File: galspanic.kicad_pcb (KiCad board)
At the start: 2 copper layers, 86.5 x 150 mm, 26 parts, among them J1 x68000_expansion, U1 CY62167E, U10 SN74AHCT245, U11 SN74AHCT245, U2 CY62167E, U3 CY62167E, U4 CY62167E, U5 ATF22V10C-10PU, U6 SN74AHCT245, U7 SN74AHCT245, U8 SN74AHCT245, U9 SN74AHCT245

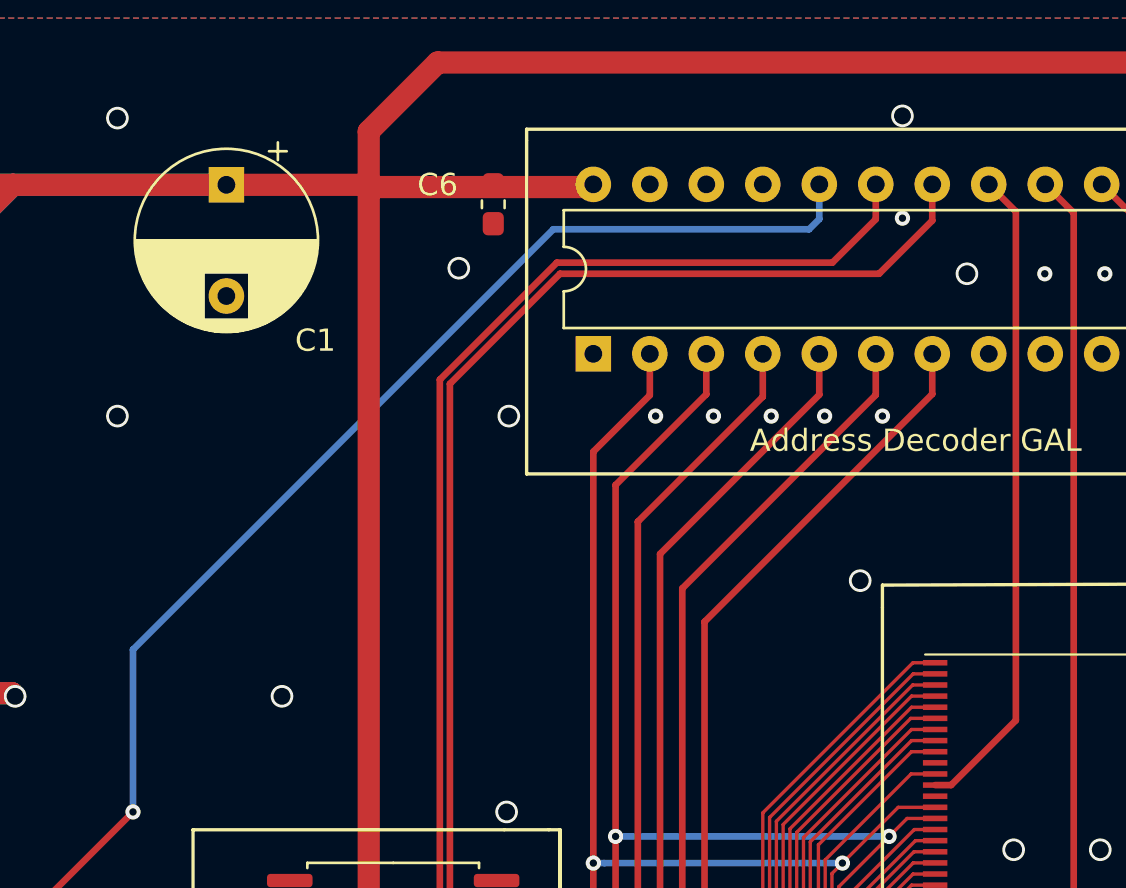
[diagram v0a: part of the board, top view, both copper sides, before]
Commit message: route A20, fix power cap footprint
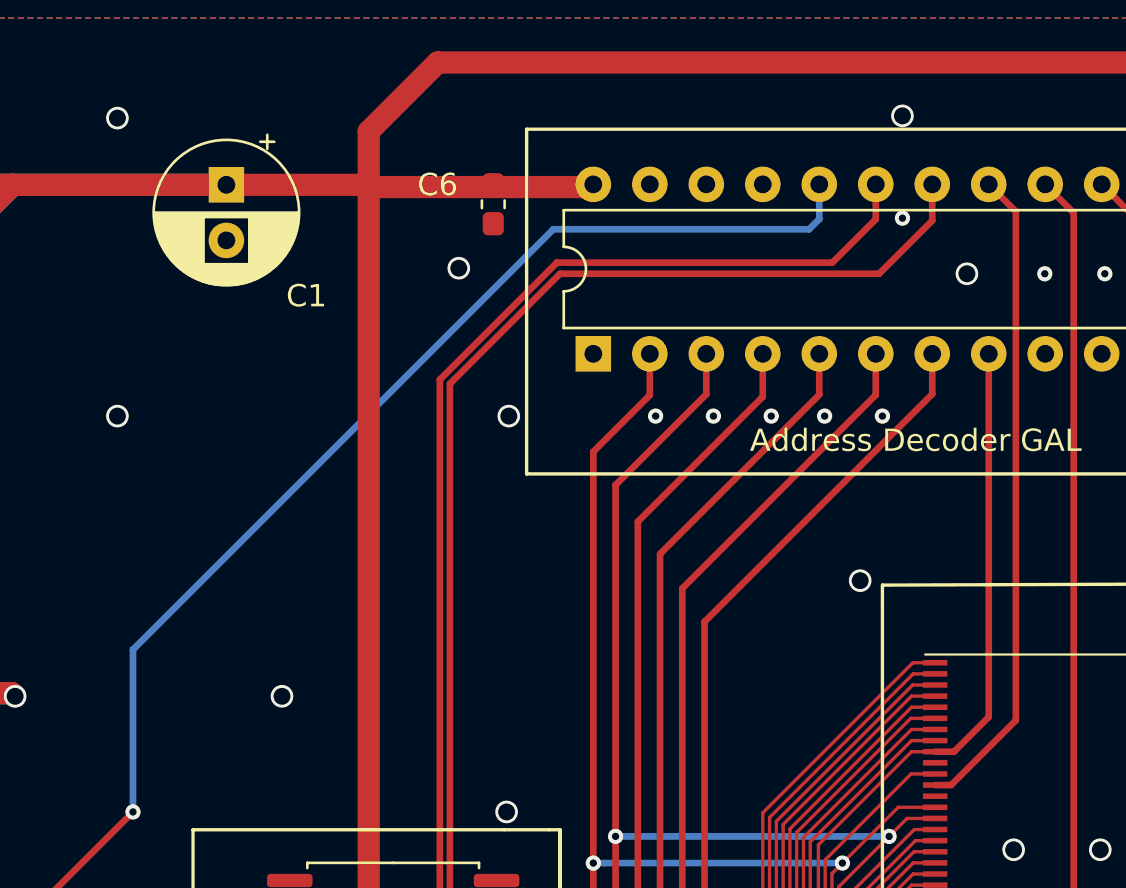
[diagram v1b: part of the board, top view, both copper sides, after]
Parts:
- C1: footprint Capacitor_THT:CP_Radial_D8.0mm_P5.00mm -> Capacitor_THT:CP_Radial_D6.3mm_P2.50mm
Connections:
- U5 pad 8: GND -> /A20
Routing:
- net /A20: track 116.5 -> 135.9 mm

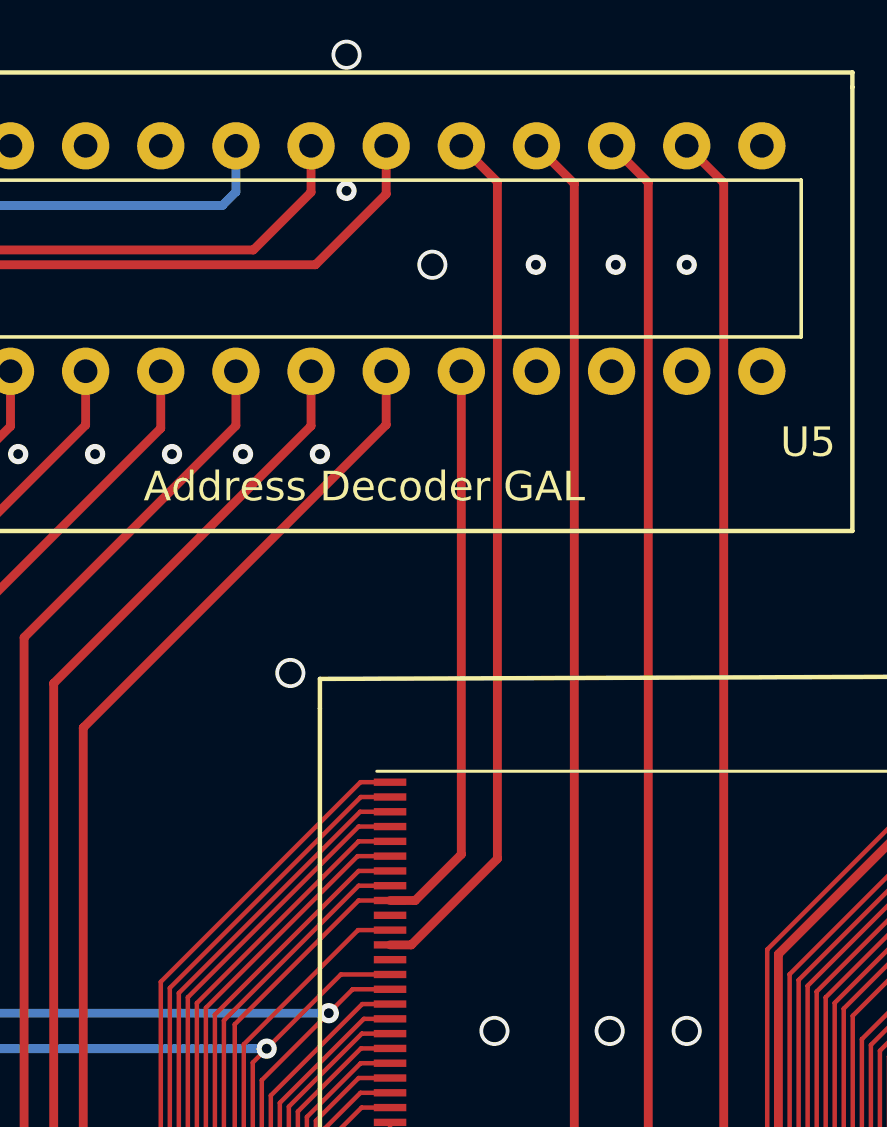
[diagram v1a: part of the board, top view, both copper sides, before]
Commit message: pcb: add grounding around A20
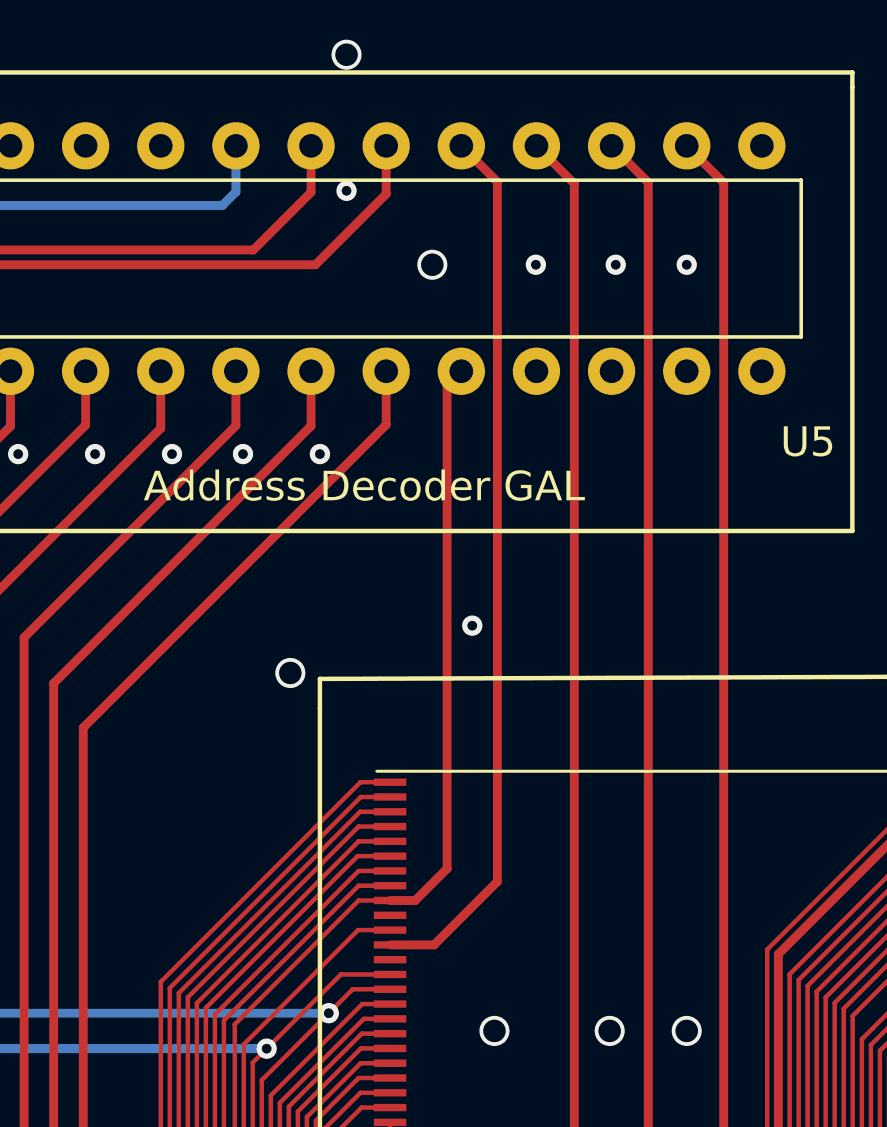
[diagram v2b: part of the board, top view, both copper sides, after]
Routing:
- net GND: vias 129 -> 130
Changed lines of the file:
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@@
     (thickness 1.6002)
     (drawings 51)
-    (tracks 1699)
+    (tracks 1701)
     (modules 26)
     (nets 155)
@@
       (edge_connector bevelled)
     )
-    (last_trace_width 0.3)
+    (last_trace_width 0.1524)
     (user_trace_width 0.3)
     (user_trace_width 1)
@@
   (gr_line (start 58 39) (end 126.5 39) (layer "Edge.Cuts") (width 0.05))
   (gr_line (start 130.5 43) (end 130.5 185) (layer "Edge.Cuts") (width 0.05))
-  (segment (start 101.78 56.6) (end 101.78 72.932604) (width 0.3) (layer "F.Cu") (net 121))
-  (segment (start 101.78 72.932604) (end 100.220868 74.491736) (width 0.3) (layer "F.Cu") (net 121))
+  (segment (start 99.370868 75.991736) (end 100.858264 75.991736) (width 0.3) (layer "F.Cu") (net 152))
+  (segment (start 100.858264 75.991736) (end 103 73.85) (width 0.3) (layer "F.Cu") (net 152))
+  (segment (start 103 73.85) (end 103 50.2) (width 0.3) (layer "F.Cu") (net 152))
+  (segment (start 103 50.2) (end 101.78 48.98) (width 0.3) (layer "F.Cu") (net 152))
+  (segment (start 119.079132 155.7) (end 118.870868 155.491736) (width 0.3) (layer "F.Cu") (net 1))
+  (segment (start 120.3 155.7) (end 119.079132 155.7) (width 0.3) (layer "F.Cu") (net 1))
+  (segment (start 101.78 56.6) (end 101.3 57.08) (width 0.3) (layer "F.Cu") (net 121))
+  (segment (start 101.3 57.08) (end 101.3 73.412604) (width 0.3) (layer "F.Cu") (net 121))
+  (segment (start 101.3 73.412604) (end 100.220868 74.491736) (width 0.3) (layer "F.Cu") (net 121))
   (segment (start 100.220868 74.491736) (end 99.370868 74.491736) (width 0.3) (layer "F.Cu") (net 121))
+  (via (at 102.15 65.2) (size 0.6858) (drill 0.3302) (layers "F.Cu" "B.Cu") (net 1))
   (segment (start 99.370868 95.491736) (end 99.370868 94.170868) (width 0.1524) (layer "F.Cu") (net 130))
   (segment (start 99.370868 94.170868) (end 91.620868 86.420868) (width 0.1524) (layer "F.Cu") (net 130))
@@
   (segment (start 103.827569 99.24932) (end 103.827569 93.05068) (width 0.1524) (layer "F.Cu") (net 115))
   (segment (start 100.585153 102.491736) (end 103.827569 99.24932) (width 0.1524) (layer "F.Cu") (net 115))
-  (segment (start 99.370868 75.991736) (end 100.089796 75.991736) (width 0.3) (layer "F.Cu") (net 152) (status 8000))
-  (segment (start 103 73.081532) (end 103 50.2) (width 0.3) (layer "F.Cu") (net 152) (status 8000))
-  (segment (start 100.089796 75.991736) (end 103 73.081532) (width 0.3) (layer "F.Cu") (net 152) (status 8000))
-  (segment (start 103 50.2) (end 101.78 48.98) (width 0.3) (layer "F.Cu") (net 152) (status 8000))
   (via (at 72.5 171.4) (size 0.6858) (drill 0.3302) (layers "F.Cu" "B.Cu") (net 143))
   (via (at 75.9 171.4) (size 0.6858) (drill 0.3302) (layers "F.Cu" "B.Cu") (net 143))
@@
   (via (at 120.4 130.7) (size 0.6858) (drill 0.3302) (layers "F.Cu" "B.Cu") (net 1))
   (segment (start 118.870868 155.491736) (end 118.870868 156.491736) (width 0.3) (layer "F.Cu") (net 1))
-  (segment (start 120.3 155.7) (end 119.079132 155.7) (width 0.3) (layer "F.Cu") (net 1))
-  (segment (start 119.079132 155.7) (end 118.870868 155.491736) (width 0.3) (layer "F.Cu") (net 1))
   (via (at 120.3 155.75) (size 0.6858) (drill 0.3302) (layers "F.Cu" "B.Cu") (net 1))
   (segment (start 112.87809 76.984514) (end 117.870868 71.991736) (width 0.1524) (layer "F.Cu") (net 90))

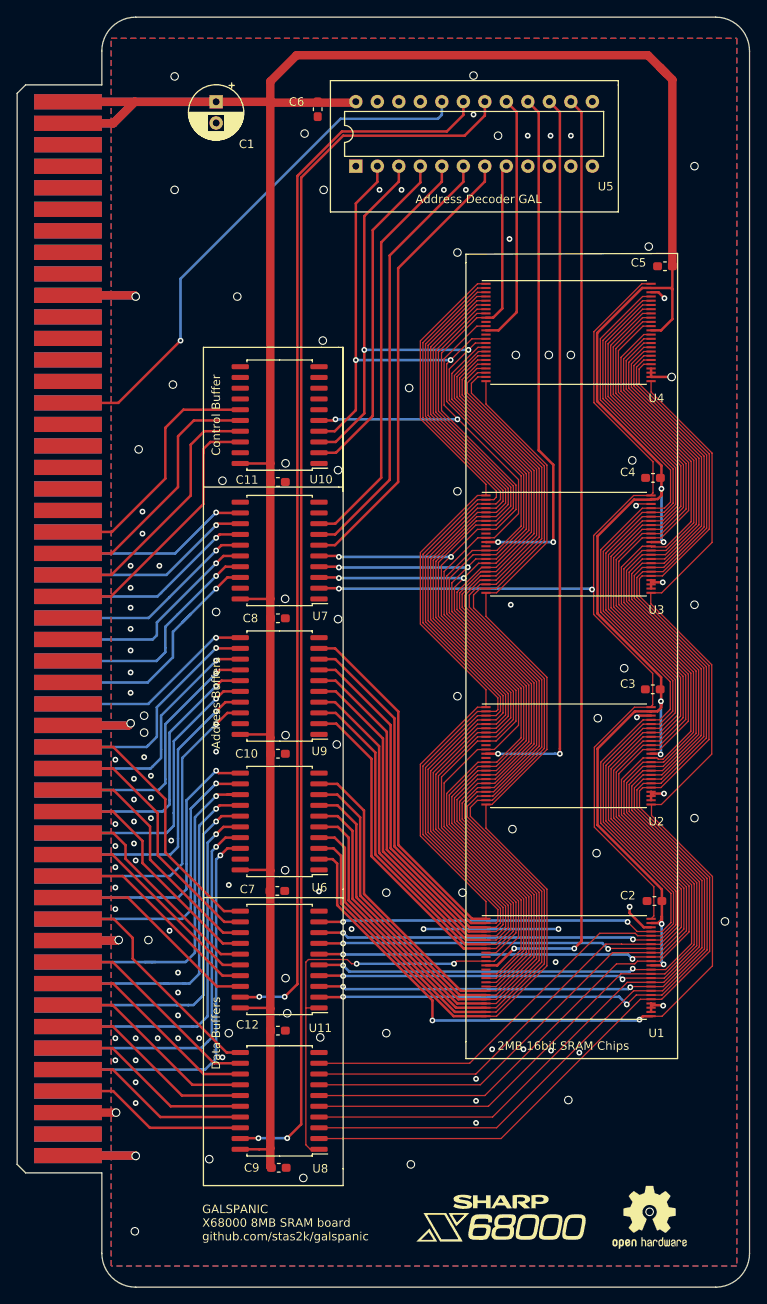
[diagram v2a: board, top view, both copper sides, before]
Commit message: pcb: add memory size jumpers
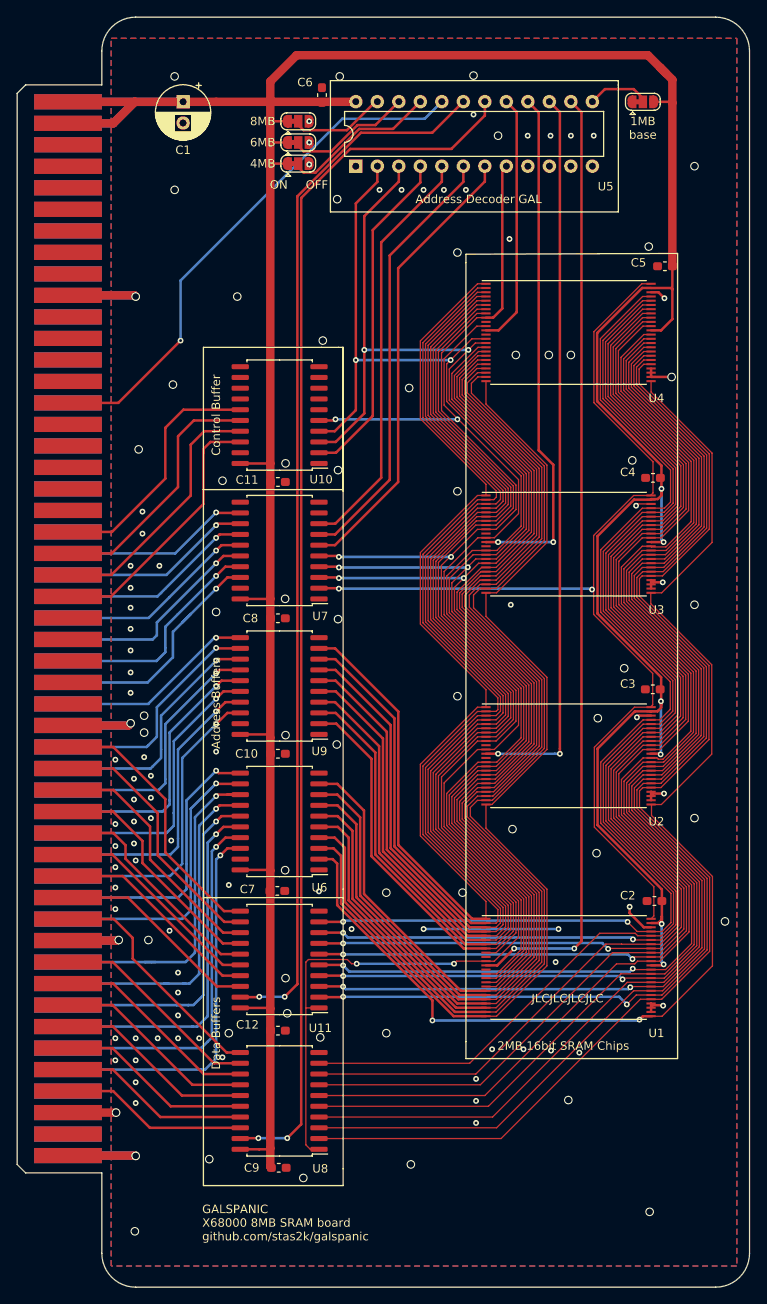
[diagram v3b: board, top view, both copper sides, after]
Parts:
- removed G***: LOGO, galspanic:x68000_logo
- removed REF**: OSHW-Logo2_9.8x8mm_SilkScreen, Symbol:OSHW-Logo2_9.8x8mm_SilkScreen
- added JP1: SolderJumper_3_Bridged12, Jumper:SolderJumper-3_P1.3mm_Bridged12_RoundedPad1.0x1.5mm, F.Cu at (77.2, 51.3)
- added JP2: SolderJumper_3_Bridged12, Jumper:SolderJumper-3_P1.3mm_Bridged12_RoundedPad1.0x1.5mm, F.Cu at (77.2, 53.8)
- added JP3: SolderJumper_3_Bridged12, Jumper:SolderJumper-3_P1.3mm_Bridged12_RoundedPad1.0x1.5mm, F.Cu at (77.2, 56.3)
- added JP4: SolderJumper_3_Bridged12, Jumper:SolderJumper-3_P1.3mm_Bridged12_RoundedPad1.0x1.5mm, F.Cu at (117.9, 49.0)
- moved C1 3.90 mm to (63.6, 49.0)
- moved C6 1.75 mm to (80.0, 48.2), turned to 90 degrees
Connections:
- net /#R/W renamed /#R/W
- net /B_R/W renamed /B_R/W
- net Net-(J1-PadA31) renamed no_connect_123
- net Net-(J1-PadB2) renamed no_connect_124
- net Net-(J1-PadB3) renamed no_connect_125
- net Net-(J1-PadB30) renamed no_connect_126
- net Net-(J1-PadB31) renamed no_connect_127
- net Net-(J1-PadB32) renamed no_connect_128
- net Net-(J1-PadB33) renamed no_connect_129
- net Net-(J1-PadB34) renamed no_connect_130
- net Net-(J1-PadB35) renamed no_connect_131
- net Net-(J1-PadB36) renamed no_connect_132
- net Net-(J1-PadB37) renamed no_connect_133
- net Net-(J1-PadB38) renamed no_connect_134
- net Net-(J1-PadB39) renamed no_connect_135
- net Net-(J1-PadB4) renamed no_connect_136
- net Net-(J1-PadB40) renamed no_connect_137
- net Net-(J1-PadB42) renamed no_connect_138
- net Net-(J1-PadB43) renamed no_connect_139
- net Net-(J1-PadB44) renamed no_connect_140
- net Net-(J1-PadB45) renamed no_connect_141
- net Net-(J1-PadB46) renamed no_connect_142
- net Net-(J1-PadB47) renamed no_connect_143
- net Net-(J1-PadB48) renamed no_connect_144
- net Net-(U1-Pad10) renamed no_connect_145
- net Net-(U1-Pad13) renamed no_connect_146
- net Net-(U10-Pad7) renamed no_connect_147
- net Net-(U10-Pad8) renamed no_connect_148
- net Net-(U10-Pad9) renamed no_connect_149
- net Net-(U2-Pad10) renamed no_connect_150
- net Net-(U2-Pad13) renamed no_connect_151
- net Net-(U3-Pad10) renamed no_connect_152
- net Net-(U3-Pad13) renamed no_connect_153
- net Net-(U4-Pad10) renamed no_connect_154
- net Net-(U4-Pad13) renamed no_connect_155
- U5 pad 13: GND -> /MSK
- U5 pad 21: Net-(U5-Pad21) -> /MS4
- U5 pad 22: Net-(U5-Pad22) -> /MS6
- U5 pad 23: Net-(U5-Pad23) -> /MS8
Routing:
- net /MS4: track 0.00 -> 18.6 mm
- net /MS6: track 0.00 -> 15.0 mm
- net /MS8: track 0.00 -> 11.9 mm
- net /MSK: track 0.00 -> 7.44 mm
- net VCC: track 429.9 -> 434.3 mm
- net /#CEH: track 127.0 -> 124.7 mm
- net /#CEL: track 146.1 -> 144.7 mm
- net /B_#DTACK: track 64.1 -> 63.1 mm
- net GND: vias 130 -> 134
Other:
- net class Default removed
- board text added: "1MB base"
- board text added: "4MB"
- board text added: "6MB"
- board text added: "8MB"
- board text added: "JLCJLCJLCJLC"
- board text added: "OFF"
- board text added: "ON"

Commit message: pcb: v1.2 release
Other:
- board text added: "GALSPANIC v1.2 X68000 8MB SRAM board github.com/stas2k/galspanic"
- board text removed: "GALSPANIC X68000 8MB SRAM board github.com/stas2k/galspanic"
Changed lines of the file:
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@@
       (viasonmask false)
       (mode 1)
-      (useauxorigin false)
+      (useauxorigin true)
       (hpglpennumber 1)
       (hpglpenspeed 20)
@@
       (drillshape 0)
       (scaleselection 1)
-      (outputdirectory "gerbers/galspanic_rel1/")
+      (outputdirectory "gerbers/galspanic-v1.2-gerbers")
     )
   )
@@
     (effects (font (size 1 1) (thickness 0.15)))
   )
-  (gr_text "GALSPANIC\nX68000 8MB SRAM board\ngithub.com/stas2k/galspanic" (at 65.85 181.4) (layer "F.SilkS")
+  (gr_text "GALSPANIC v1.2\nX68000 8MB SRAM board\ngithub.com/stas2k/galspanic" (at 65.85 181.4) (layer "F.SilkS")
     (effects (font (size 1 1) (thickness 0.15)) (justify left))
   )
